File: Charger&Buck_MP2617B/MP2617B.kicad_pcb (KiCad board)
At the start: 2 copper layers, 50.2 x 17.5 mm, 43 parts, among them J1 Jumper

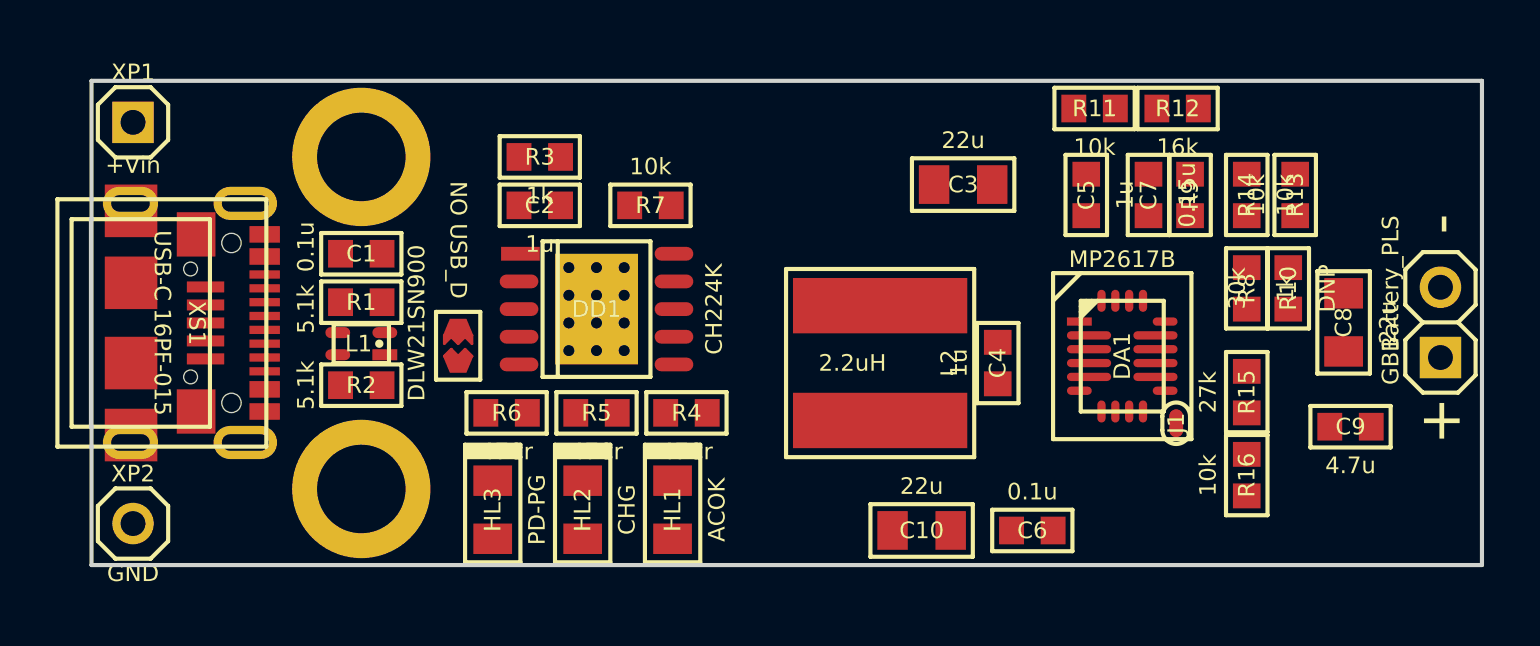
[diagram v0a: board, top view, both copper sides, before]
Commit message: трассирровка завершкна, шелкография сделана.
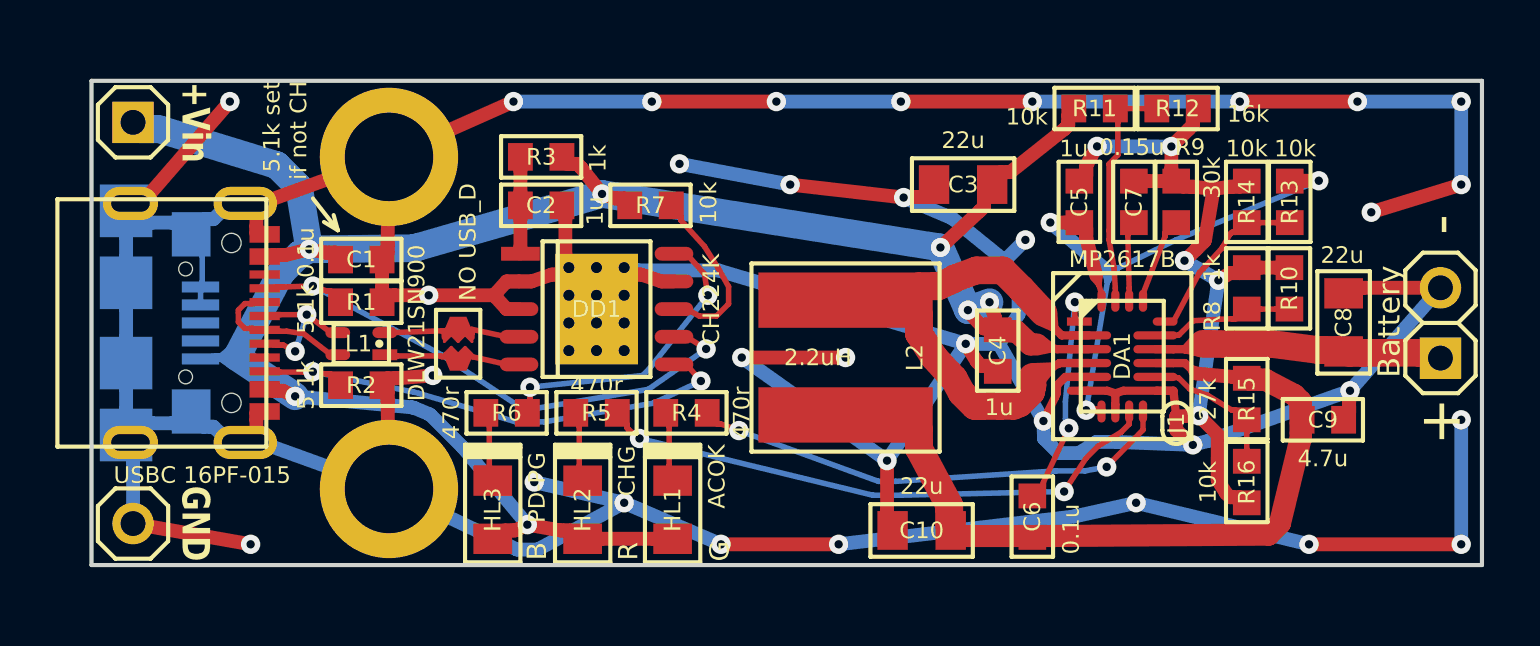
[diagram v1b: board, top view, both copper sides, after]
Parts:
- GB1: value Battery_PLS -> Battery
- XS1: value USB-C 16PF-015 -> USBC 16PF-015
- XS2: moved to B.Cu
- moved L2 1.27 mm to (127.2, 92.5)
- moved C9 1.03 mm to (144.5, 94.8)
- moved Hole1 1.00 mm to (110.8, 85.2)
- moved Hole2 1.00 mm to (110.8, 97.2)
- moved C7 0.58 mm to (137.7, 86.9)
- moved R9 0.56 mm to (139.2, 86.9)
- moved C6 0.50 mm to (134.0, 98.2), turned to -90 degrees
- moved C4 0.45 mm to (132.8, 92.2)
- moved C5 0.35 mm to (135.7, 86.9)
- moved R13 0.32 mm to (143.3, 86.9)
- moved R14 0.25 mm to (141.8, 86.9)
- moved R15 0.25 mm to (141.8, 94.0)
- moved R16 0.25 mm to (141.8, 97.0)
- moved C1 0.21 mm to (109.8, 89.0)
- moved XS2 0.18 mm to (101.2, 91.2)
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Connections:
- net /LX1 renamed /+LX1
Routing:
- net GNDP: track 0.00 -> 246.9 mm, vias 0 -> 33
- net +USBvcc: track 0.00 -> 83.6 mm, vias 0 -> 7
- net GND: track 0.00 -> 33.4 mm, vias 0 -> 5
- net +VCC: track 0.00 -> 29.5 mm
- net /+LX1: track 0.00 -> 24.4 mm
- net /MP_VCC: track 0.00 -> 23.8 mm, vias 0 -> 3
- net /CHG: track 0.00 -> 20.8 mm, vias 0 -> 2
- net /USB_CC1: track 0.00 -> 20.2 mm, vias 0 -> 2
- net /USB_CC2: track 0.00 -> 18.7 mm, vias 0 -> 2
- net /ACOK: track 0.00 -> 17.5 mm, vias 0 -> 2
- net /+BATT: track 0.00 -> 11.6 mm
- net /CH_PG: track 0.00 -> 11.0 mm, vias 0 -> 2
- net /VLIM: track 0.00 -> 8.61 mm
- net Net-(DA1-BST): track 0.00 -> 8.25 mm, vias 0 -> 2
- net /CH_DP: track 0.00 -> 6.59 mm
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- added copper zone on B.Cu, net GNDP
- added copper zone on F.Cu, net GNDP
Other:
- board text added: "+Vin"
- board text added: "5.1k set if not CH"
- board text added: "B"
- board text added: "Battery"
- board text added: "G"
- board text added: "GND"
- board text added: "R"
- board text added: "R8"
- board text added: "R8 Ichg, A 680r ~3.0 820r ~2.5 1k ~2.1A 1.3k ~1.6A 2k ~1.0A"
- board text added: "R9"
- board text added: "R9 Iin_lim, A 51k ~0.9A 30k ~1.5A 22k ~2.1A 18k ~2.5A 15k ~3A"
- board text added: "«MP2617B module»"

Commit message: исправления и дополнения
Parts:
- R4, R5, R6: value 470r -> 1k
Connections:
- C1 pad 2: GNDP -> GND
- C10 pad 2: GNDP -> GND
- C2 pad 2: GNDP -> GND
- C3 pad 2: GNDP -> GND
- C4 pad 2: GNDP -> GND
- C5 pad 1: /MP_VCC -> /+MP_VCC
- C5 pad 2: GND -> GNDL
- C7 pad 2: GND -> GNDL
- C8 pad 2: GNDP -> GND
- C9 pad 2: GNDP -> GND
- DA1 pad 11: GND -> GNDL
- DA1 pad 20: /MP_VCC -> /+MP_VCC
- DA1 pad 5: GNDP -> GND
- DA1 pad 6: GND -> GNDL
- DA1 pad 7: /MP_VCC -> /+MP_VCC
- DA1 pad 8: GND -> GNDL
- DD1 pad PAD: GNDP -> GND
- GB1 pad 2: GNDP -> GND
- Hole1 pad H: GNDP -> GND
- Hole2 pad H: GNDP -> GND
- J1 pad 1: GND -> GNDL
- J1 pad 2: GNDP -> GND
- R1 pad 2: GNDP -> GND
- R10 pad 2: GND -> GNDL
- R12 pad 2: GND -> GNDL
- R14 pad 2: GND -> GNDL
- R16 pad 2: GND -> GNDL
- R2 pad 2: GNDP -> GND
- R8 pad 2: GND -> GNDL
- R9 pad 2: GND -> GNDL
- XP2 pad 1: GNDP -> GND
- XS1 pad A1B12: GNDP -> GND
- XS1 pad B1A12: GNDP -> GND
- XS1 pad SHLD: GNDP -> GND
- XS2 pad 4: GNDP -> GND
- XS2 pad 5: GNDP -> GND
- XS2 pad SHLD: GNDP -> GND
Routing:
- net GNDL: track 0.00 -> 33.4 mm, vias 0 -> 5
- net GND: track 33.4 -> 0.00 mm, vias 5 -> 0
